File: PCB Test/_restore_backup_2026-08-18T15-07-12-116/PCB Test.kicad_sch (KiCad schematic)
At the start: 39 parts, among them J1 Screw_Terminal_01x02, J5 Screw_Terminal_01x02, J6 Conn_02x03_Odd_Even, Q2 NMOS, Q3 NMOS, SW1 SW_Push, U1 ATmega4808-A, U2 TCRT5000, U3 TCRT5000, U4 TCRT5000, U5 MCP1700x-330xxTO

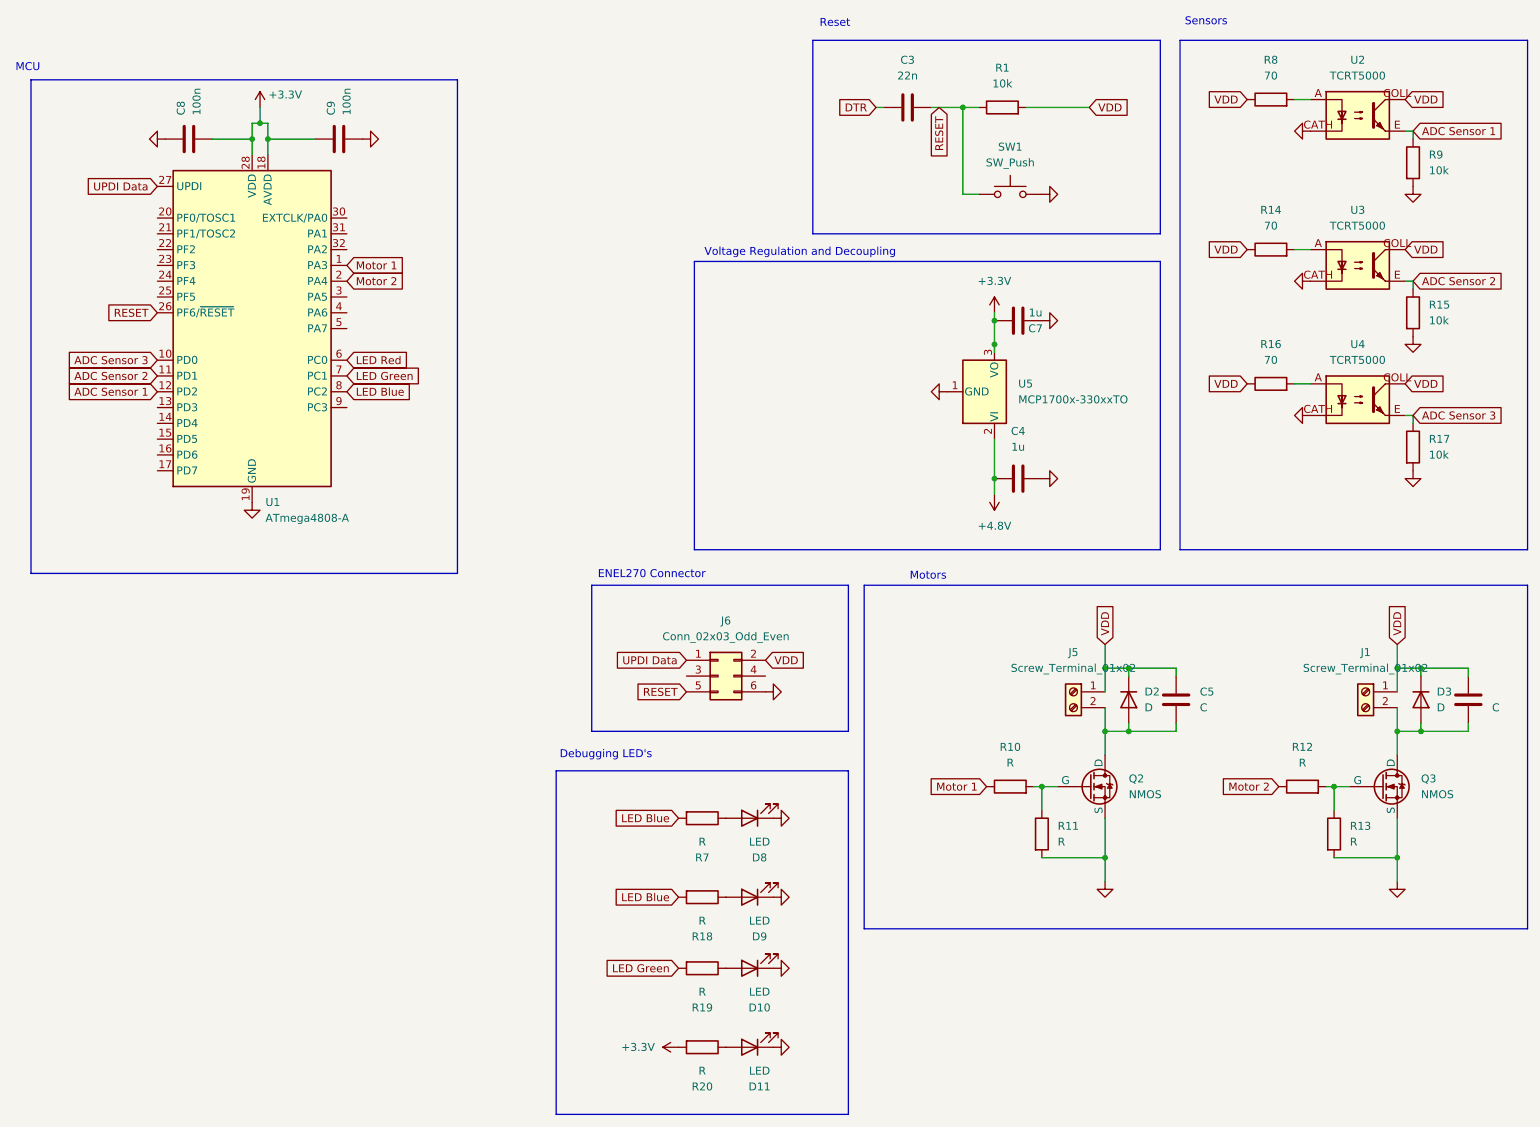
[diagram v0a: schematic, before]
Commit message: Added LED's, voltage, repositioned decoupling capacitors
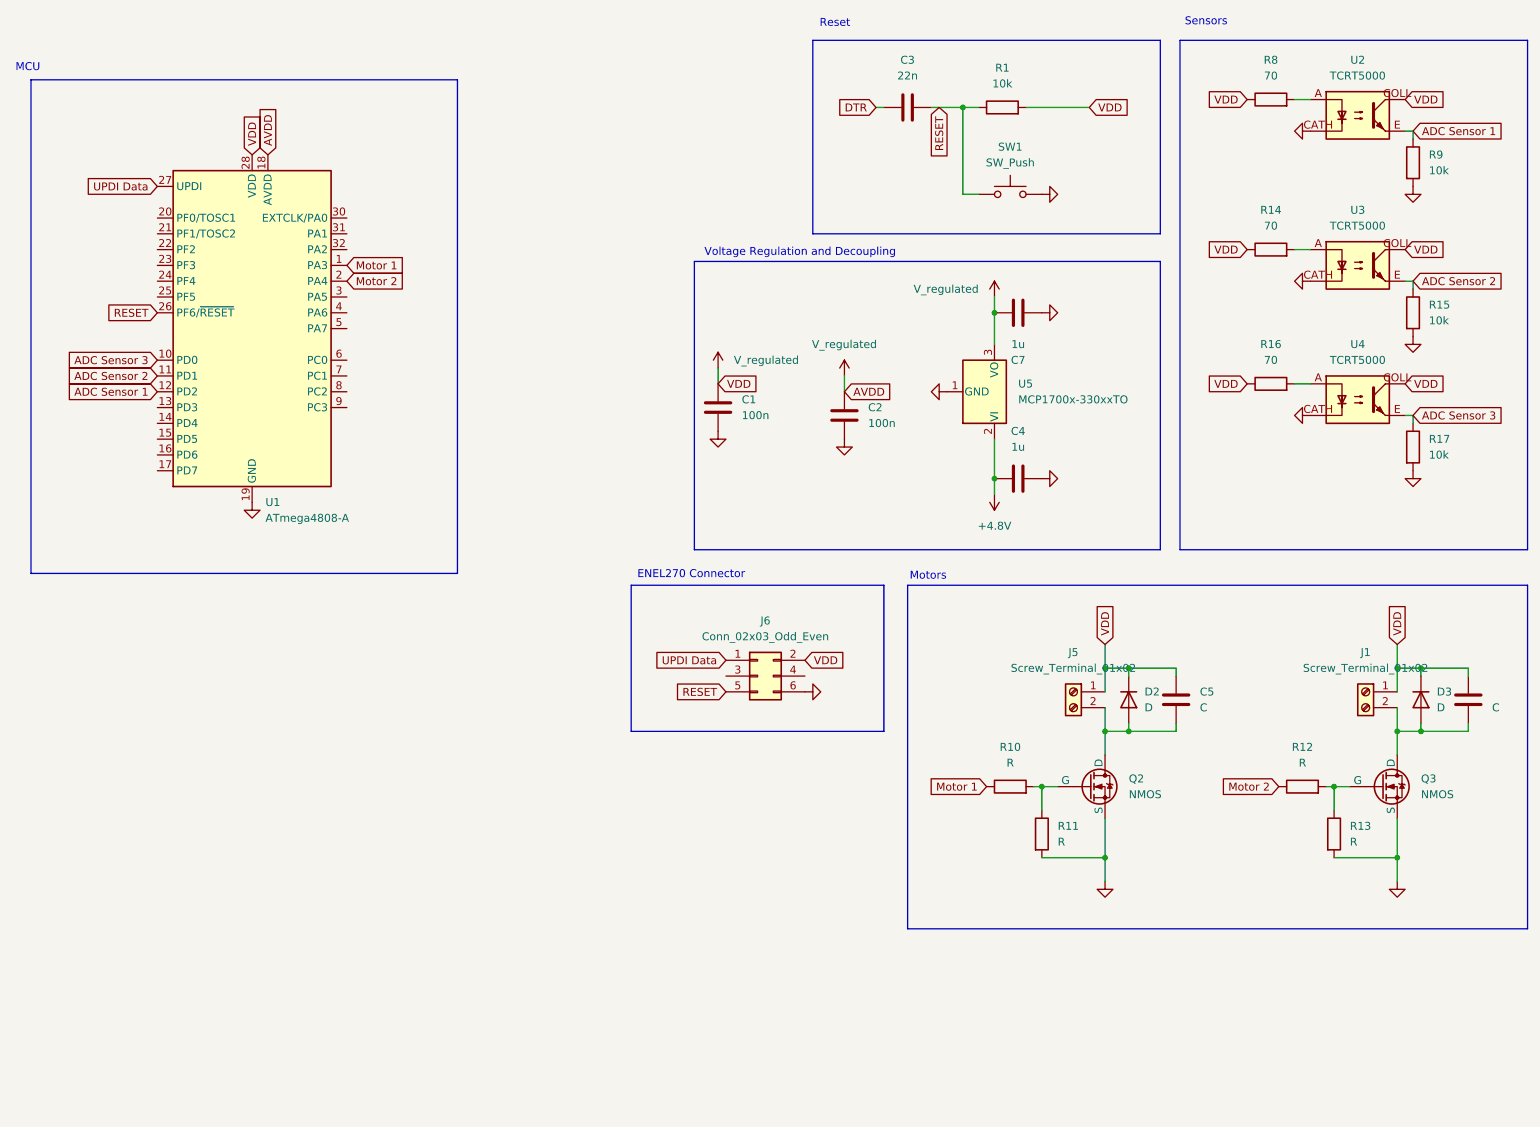
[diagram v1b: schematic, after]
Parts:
- removed C8, C9: 100n, symbol Device:C
- removed D10, D11, D8, D9: LED, symbol Device:LED
- removed R18, R19, R20, R7: R, symbol Device:R
- added C1, C2: 100n, symbol Device:C
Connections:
- net VDD is gone; now on net V_regulated: C5.1, C6.1, D2.1 (K), D3.1 (K), J1.1 (Pin_1), J5.1 (Pin_1), J6.2 (Pin_2), R1.2, R14.1, R16.1, R8.1, U2.COLL, U3.COLL, U4.COLL
- net GND: now also C1.2, C2.2
- net +3.3V renamed V_regulated
- net V_regulated: now also C1.1, C2.1
- net LED Blue: no longer names the net of U1.8 (PC2)
- net LED Green: no longer names the net of U1.7 (PC1)
- net LED Red: no longer names the net of U1.6 (PC0)
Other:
- note removed: "Debugging LED's"
- moved on the sheet: C7, J6
